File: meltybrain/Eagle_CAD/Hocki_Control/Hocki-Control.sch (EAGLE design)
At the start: 113 parts, among them J1 SM03B-SRSS-TB(LF)(SN), J2 SM03B-SRSS-TB(LF)(SN), U1 TEENSY_4.1, U10 TLV3502AIDCNR, U11 NL27WZ32USG, U12 NL27WZ32USG, U13 HMC1052L-TR, U14 LMV358, U15 IRF7509, U16 TMUX1219DCKR, U17 LMV358, U18 LMV358, U19 AP2210K-3.3TRG1, U2 ADXL375, U20 AP2210K-5.0TRG1, U21 MAX20075ATCA/V+, U3 ADXL375, U4 ADXL375, U5 ADXL375, U6 LMH6612MAX/NOPB, U7 LMH6612MAX/NOPB, U8 LMH6612MAX/NOPB, U9 LMH6612MAX/NOPB

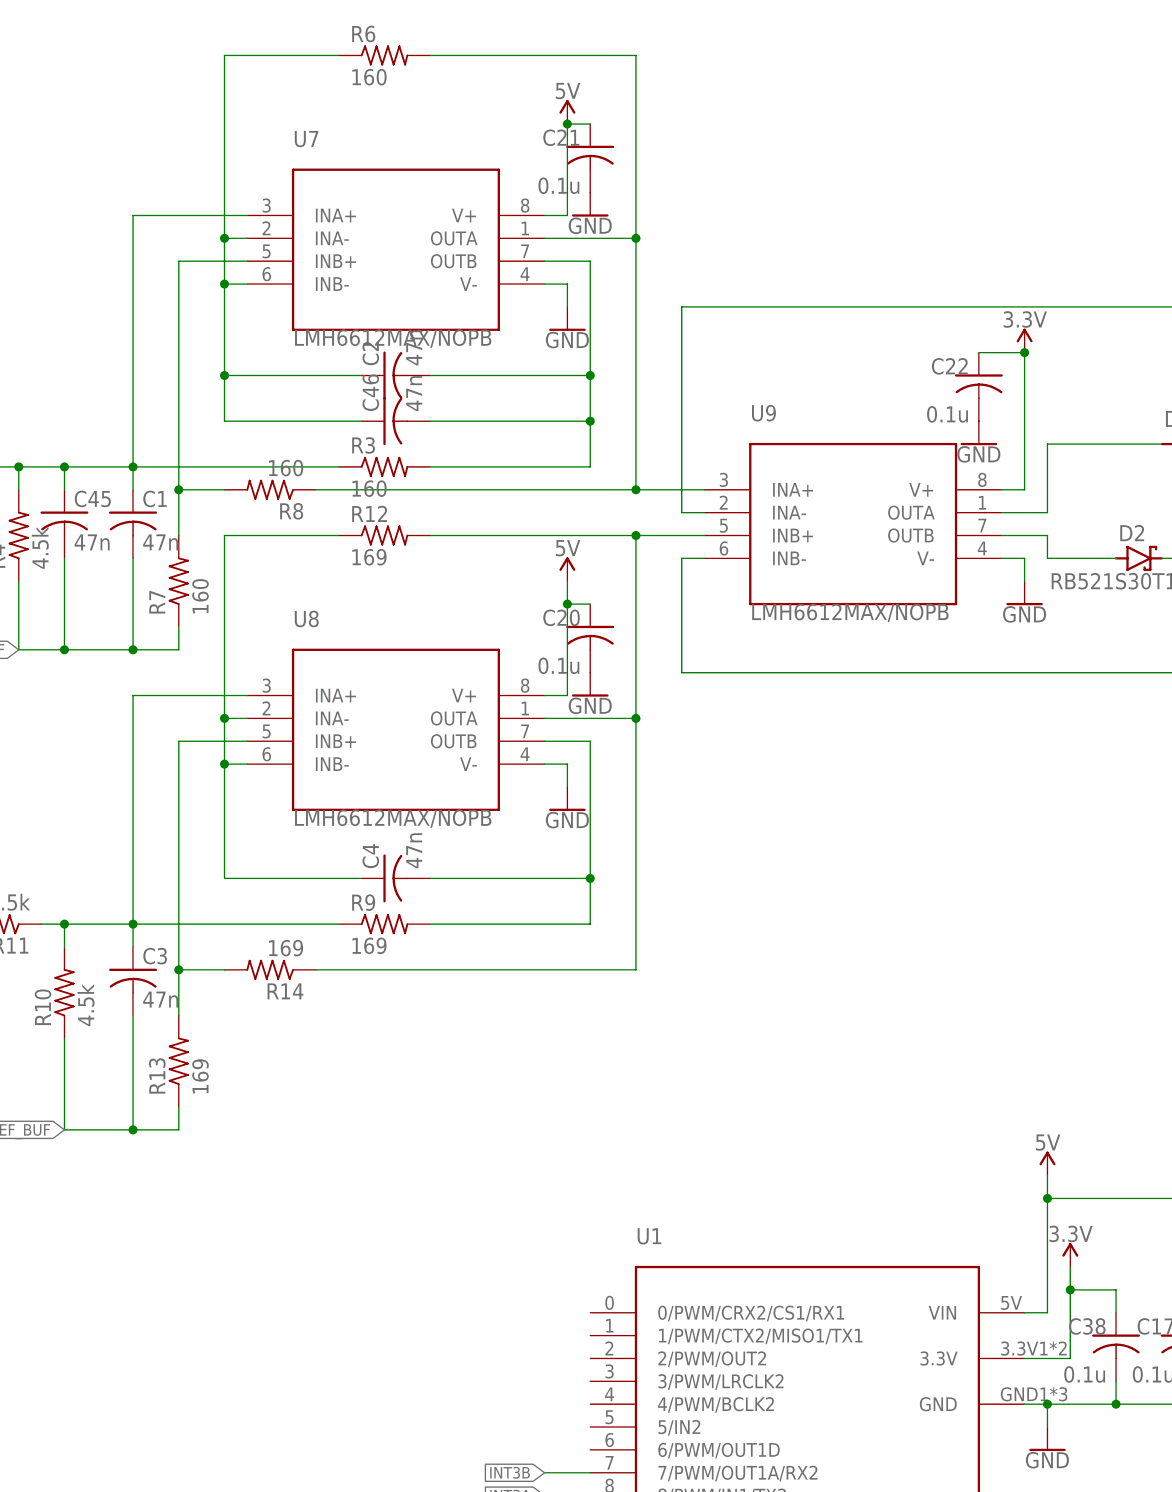
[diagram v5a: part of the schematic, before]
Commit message: errr---added a connector
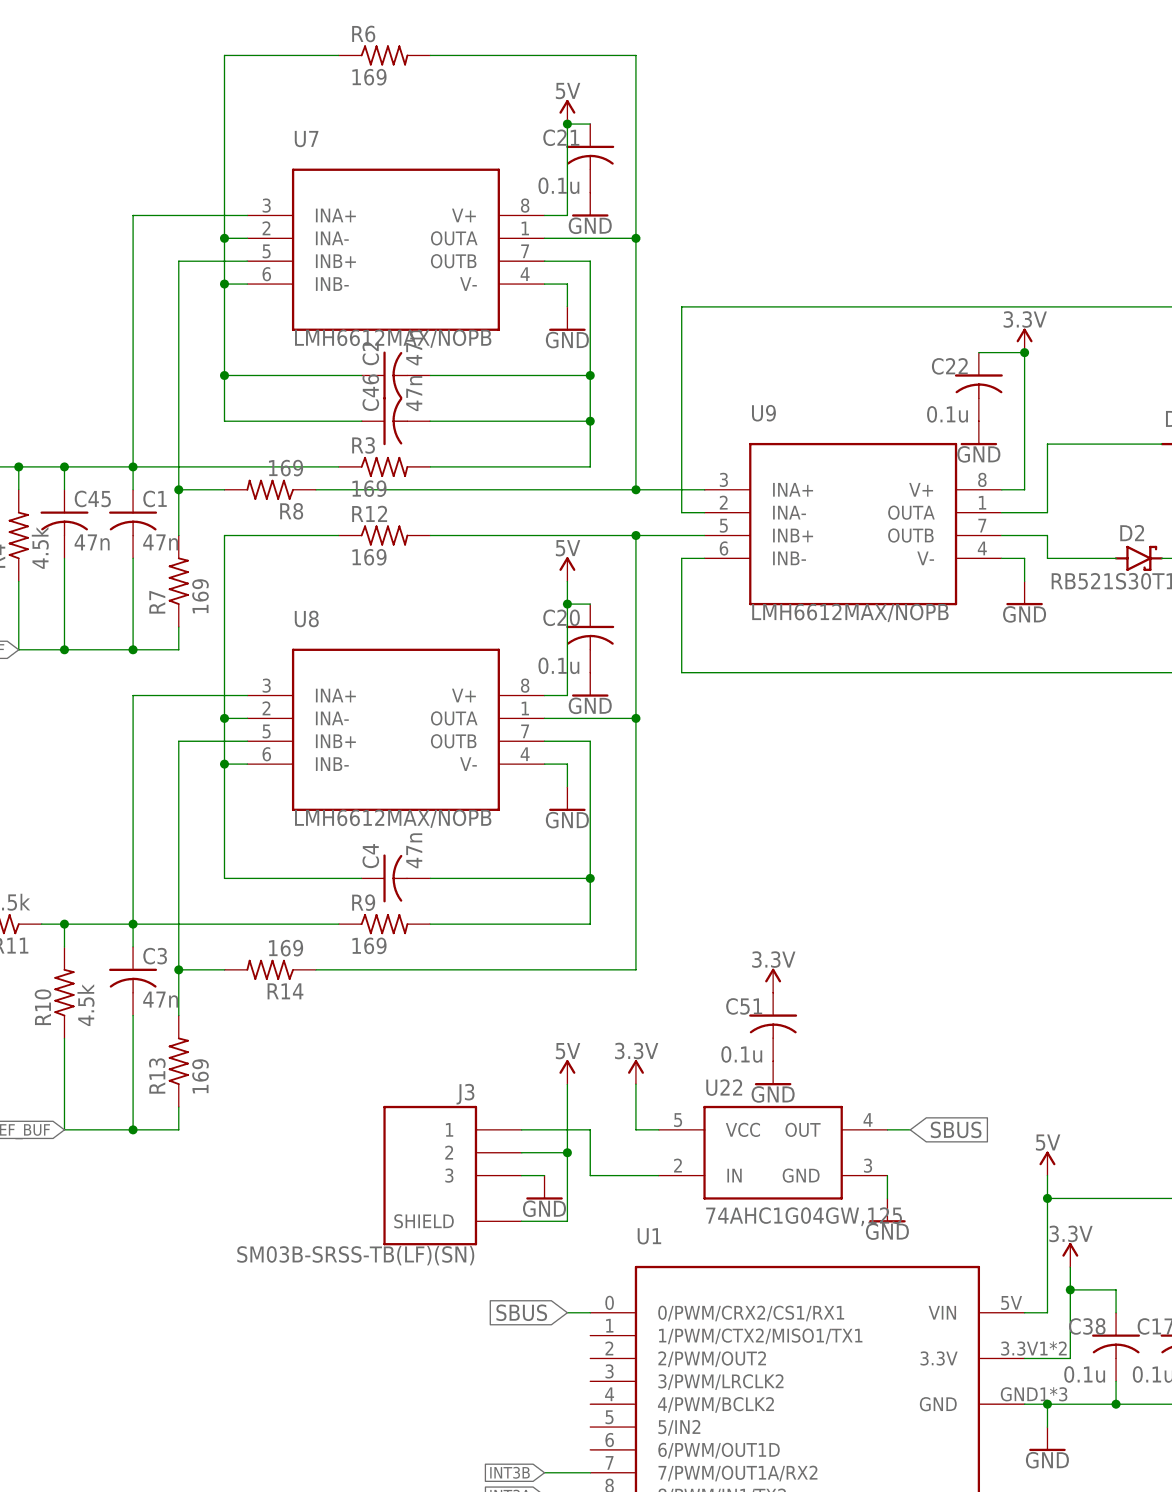
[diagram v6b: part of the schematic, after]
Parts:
- added C51: 0.1u, rcl:C-USC0603
- added J3: SM03B-SRSS-TB(LF)(SN), Hocki_Library:SM03B-SRSS-TB(LF)(SN)
- added U22: 74AHC1G04GW,125, Hocki_Library:74AHC1G04GW,125
- R3, R6, R7, R8: value 160 -> 169
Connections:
- new net N$17: J3.1, U22.IN
- new net SBUS: U1.0/PWM/CRX2/CS1/RX1, U22.OUT
- net 3.3V: now also C51.1, U22.VCC
- net 5V: now also J3.2, J3.SHIELD
- net GND: now also C51.2, J3.3, U22.GND
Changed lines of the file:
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@@
 <part name="SUPPLY5" library="SparkFun-PowerSymbols" library_urn="urn:adsk.eagle:library:530" deviceset="5V" device=""/>
 <part name="GND5" library="SparkFun-PowerSymbols" library_urn="urn:adsk.eagle:library:530" deviceset="GND" device=""/>
-<part name="R3" library="rcl" library_urn="urn:adsk.eagle:library:334" deviceset="R-US_" device="R0603" package3d_urn="urn:adsk.eagle:package:23555/3" value="160"/>
+<part name="R3" library="rcl" library_urn="urn:adsk.eagle:library:334" deviceset="R-US_" device="R0603" package3d_urn="urn:adsk.eagle:package:23555/3" value="169"/>
 <part name="R4" library="rcl" library_urn="urn:adsk.eagle:library:334" deviceset="R-US_" device="R0603" package3d_urn="urn:adsk.eagle:package:23555/3" value="4.5k"/>
 <part name="R5" library="rcl" library_urn="urn:adsk.eagle:library:334" deviceset="R-US_" device="R0603" package3d_urn="urn:adsk.eagle:package:23555/3" value="4.5k"/>
 <part name="GND7" library="SparkFun-PowerSymbols" library_urn="urn:adsk.eagle:library:530" deviceset="GND" device=""/>
 <part name="SUPPLY6" library="SparkFun-PowerSymbols" library_urn="urn:adsk.eagle:library:530" deviceset="5V" device=""/>
-<part name="R6" library="rcl" library_urn="urn:adsk.eagle:library:334" deviceset="R-US_" device="R0603" package3d_urn="urn:adsk.eagle:package:23555/3" value="160"/>
-<part name="R7" library="rcl" library_urn="urn:adsk.eagle:library:334" deviceset="R-US_" device="R0603" package3d_urn="urn:adsk.eagle:package:23555/3" value="160"/>
-<part name="R8" library="rcl" library_urn="urn:adsk.eagle:library:334" deviceset="R-US_" device="R0603" package3d_urn="urn:adsk.eagle:package:23555/3" value="160"/>
+<part name="R6" library="rcl" library_urn="urn:adsk.eagle:library:334" deviceset="R-US_" device="R0603" package3d_urn="urn:adsk.eagle:package:23555/3" value="169"/>
+<part name="R7" library="rcl" library_urn="urn:adsk.eagle:library:334" deviceset="R-US_" device="R0603" package3d_urn="urn:adsk.eagle:package:23555/3" value="169"/>
+<part name="R8" library="rcl" library_urn="urn:adsk.eagle:library:334" deviceset="R-US_" device="R0603" package3d_urn="urn:adsk.eagle:package:23555/3" value="169"/>
 <part name="U8" library="Hocki_Library" deviceset="LMH6612MAX/NOPB" device=""/>
 <part name="R9" library="rcl" library_urn="urn:adsk.eagle:library:334" deviceset="R-US_" device="R0603" package3d_urn="urn:adsk.eagle:package:23555/3" value="169"/>
@@
 <part name="GND59" library="SparkFun-PowerSymbols" library_urn="urn:adsk.eagle:library:530" deviceset="GND" device=""/>
 <part name="SUPPLY22" library="Hocki_Library" deviceset="9V" device=""/>
+<part name="J3" library="Hocki_Library" deviceset="SM03B-SRSS-TB(LF)(SN)" device=""/>
+<part name="GND60" library="SparkFun-PowerSymbols" library_urn="urn:adsk.eagle:library:530" deviceset="GND" device=""/>
+<part name="SUPPLY23" library="SparkFun-PowerSymbols" library_urn="urn:adsk.eagle:library:530" deviceset="5V" device=""/>
+<part name="U22" library="Hocki_Library" deviceset="74AHC1G04GW,125" device=""/>
+<part name="SUPPLY24" library="SparkFun-PowerSymbols" library_urn="urn:adsk.eagle:library:530" deviceset="3.3V" device=""/>
+<part name="GND61" library="SparkFun-PowerSymbols" library_urn="urn:adsk.eagle:library:530" deviceset="GND" device=""/>
+<part name="C51" library="rcl" library_urn="urn:adsk.eagle:library:334" deviceset="C-US" device="C0603" package3d_urn="urn:adsk.eagle:package:23616/2" value="0.1u"/>
+<part name="SUPPLY25" library="SparkFun-PowerSymbols" library_urn="urn:adsk.eagle:library:530" deviceset="3.3V" device=""/>
+<part name="GND62" library="SparkFun-PowerSymbols" library_urn="urn:adsk.eagle:library:530" deviceset="GND" device=""/>
 </parts>
 <sheets>
@@
 <instance part="SUPPLY22" gate="G$1" x="231.14" y="55.88" smashed="yes">
 <attribute name="VALUE" x="231.14" y="58.674" size="1.778" layer="96" align="bottom-center"/>
+</instance>
+<instance part="J3" gate="G$1" x="243.84" y="205.74" smashed="yes" rot="MR0">
+<attribute name="NAME" x="248.92" y="214.122" size="1.778" layer="95" rot="MR0"/>
+<attribute name="VALUE" x="248.92" y="197.866" size="1.778" layer="96" rot="MR0" align="top-left"/>
+</instance>
+<instance part="GND60" gate="1" x="256.54" y="203.2" smashed="yes">
+<attribute name="VALUE" x="256.54" y="202.946" size="1.778" layer="96" align="top-center"/>
+</instance>
+<instance part="SUPPLY23" gate="G$1" x="259.08" y="215.9" smashed="yes">
+<attribute name="VALUE" x="259.08" y="218.694" size="1.778" layer="96" align="bottom-center"/>
+</instance>
+<instance part="U22" gate="G$1" x="281.94" y="210.82" smashed="yes">
+<attribute name="NAME" x="274.32" y="214.63" size="1.778" layer="95" ratio="6" rot="SR0"/>
+<attribute name="VALUE" x="274.32" y="202.184" size="1.778" layer="96" ratio="6" rot="SR0" align="top-left"/>
+</instance>
+<instance part="SUPPLY24" gate="G$1" x="266.7" y="215.9" smashed="yes">
+<attribute name="VALUE" x="266.7" y="218.694" size="1.778" layer="96" align="bottom-center"/>
+</instance>
+<instance part="GND61" gate="1" x="294.64" y="200.66" smashed="yes">
+<attribute name="VALUE" x="294.64" y="200.406" size="1.778" layer="96" align="top-center"/>
+</instance>
+<instance part="C51" gate="G$1" x="281.94" y="223.52" smashed="yes">
+<attribute name="NAME" x="280.924" y="225.425" size="1.778" layer="95" rot="R180"/>
+<attribute name="VALUE" x="280.924" y="220.091" size="1.778" layer="96" rot="R180"/>
+</instance>
+<instance part="SUPPLY25" gate="G$1" x="281.94" y="226.06" smashed="yes">
+<attribute name="VALUE" x="281.94" y="228.854" size="1.778" layer="96" align="bottom-center"/>
+</instance>
+<instance part="GND62" gate="1" x="281.94" y="215.9" smashed="yes">
+<attribute name="VALUE" x="281.94" y="215.646" size="1.778" layer="96" align="top-center"/>
 </instance>
 </instances>
@@
 <pinref part="GND59" gate="1" pin="GND"/>
 </segment>
+<segment>
+<pinref part="J3" gate="G$1" pin="3"/>
+<wire x1="254" y1="205.74" x2="256.54" y2="205.74" width="0.1524" layer="91"/>
+<pinref part="GND60" gate="1" pin="GND"/>
+</segment>
+<segment>
+<pinref part="U22" gate="G$1" pin="GND"/>
+<wire x1="294.64" y1="205.74" x2="294.64" y2="203.2" width="0.1524" layer="91"/>
+<pinref part="GND61" gate="1" pin="GND"/>
+</segment>
+<segment>
+<pinref part="C51" gate="G$1" pin="2"/>
+<pinref part="GND62" gate="1" pin="GND"/>
+</segment>
 </net>
 <net name="3.3V" class="0">
@@
 <wire x1="320.04" y1="193.04" x2="314.96" y2="193.04" width="0.1524" layer="91"/>
 <junction x="314.96" y="193.04"/>
+</segment>
+<segment>
+<pinref part="U22" gate="G$1" pin="VCC"/>
+<wire x1="269.24" y1="210.82" x2="266.7" y2="210.82" width="0.1524" layer="91"/>
+<wire x1="266.7" y1="210.82" x2="266.7" y2="215.9" width="0.1524" layer="91"/>
+<pinref part="SUPPLY24" gate="G$1" pin="3.3V"/>
+</segment>
+<segment>
+<pinref part="C51" gate="G$1" pin="1"/>
+<pinref part="SUPPLY25" gate="G$1" pin="3.3V"/>
 </segment>
 </net>
@@
 <pinref part="SUPPLY20" gate="G$1" pin="5V"/>
 </segment>
+<segment>
+<pinref part="J3" gate="G$1" pin="2"/>
+<wire x1="254" y1="208.28" x2="259.08" y2="208.28" width="0.1524" layer="91"/>
+<wire x1="259.08" y1="208.28" x2="259.08" y2="215.9" width="0.1524" layer="91"/>
+<pinref part="SUPPLY23" gate="G$1" pin="5V"/>
+<pinref part="J3" gate="G$1" pin="SHIELD"/>
+<wire x1="254" y1="200.66" x2="259.08" y2="200.66" width="0.1524" layer="91"/>
+<wire x1="259.08" y1="200.66" x2="259.08" y2="208.28" width="0.1524" layer="91"/>
+<junction x="259.08" y="208.28"/>
+</segment>
 </net>
 <net name="VG_SIGNAL_BUF" class="0">
@@
 </segment>
 </net>
+<net name="N$17" class="0">
+<segment>
+<pinref part="J3" gate="G$1" pin="1"/>
+<wire x1="254" y1="210.82" x2="261.62" y2="210.82" width="0.1524" layer="91"/>
+<wire x1="261.62" y1="210.82" x2="261.62" y2="205.74" width="0.1524" layer="91"/>
+<pinref part="U22" gate="G$1" pin="IN"/>
+<wire x1="261.62" y1="205.74" x2="269.24" y2="205.74" width="0.1524" layer="91"/>
+</segment>
+</net>
+<net name="SBUS" class="0">
+<segment>
+<pinref part="U22" gate="G$1" pin="OUT"/>
+<wire x1="294.64" y1="210.82" x2="297.18" y2="210.82" width="0.1524" layer="91"/>
+<label x="297.18" y="210.82" size="1.778" layer="95" xref="yes"/>
+</segment>
+<segment>
+<pinref part="U1" gate="G$1" pin="0/PWM/CRX2/CS1/RX1"/>
+<wire x1="261.62" y1="190.5" x2="259.08" y2="190.5" width="0.1524" layer="91"/>
+<label x="259.08" y="190.5" size="1.778" layer="95" rot="R180" xref="yes"/>
+</segment>
+</net>

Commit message: finished routing control?
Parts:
- added C52: 22u, rcl:C-USC1206
- added C53: 4.7u, rcl:C-USC0603
- added C54: 1u, rcl:C-USC0603
- added CN1: (no value), Hocki_Library:JST_2PIN-SMT-RA
- added J4, J5: SM04B-SRSS-TB(LF)(SN), Hocki_Library:SM04B-SRSS-TB(LF)(SN)
- added U23: LDL212PU50R, Hocki_Library:LDL212PU50R
- C47: value 4.7u -> 10u
- C49: value 1u -> 100p
- L1: value 4.7u -> 10uH; device Hocki_Library:CBC2518T4R7M -> Hocki_Library:LQH5BPN100M38L
- R1: value 324k -> 205k
- R15: value 40.2k -> 20k
- U21: value MAX20075ATCA/V+ -> AP63200; device Hocki_Library:MAX20075ATCA/V+ -> Hocki_Library:AP63200
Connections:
- removed net N$6: C49.1, U21.BIAS
- new net +5V: C53.1, J4.1, J4.SHIELD, J5.1, J5.SHIELD, U23.ADJ/SENSE, U23.OUT
- new net LED_CLK1: J4.2, U1.2/PWM/OUT2
- new net LED_CLK2: J5.2, U1.4/PWM/BCLK2
- new net LED_DATA1: J4.3, U1.1/PWM/CTX2/MISO1/TX1
- new net LED_DATA2: J5.3, U1.3/PWM/LRCLK2
- net +24V: now also CN1.2, CN1.SHIELD, U21.IN; no longer U21.SUP
- net 9V: now also C49.1, C52.1, C54.1, U23.IN; no longer U21.OUT
- net GND: now also C52.2, C53.2, C54.2, CN1.1, J4.4, J5.4, U21.GND, U23.GND; no longer C49.2, U21.AGND, U21.EPAD, U21.PGND
- net N$12: now also C49.2
- net N$3: now also U21.SW; no longer U21.LX
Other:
- moved on the sheet: C47, C48, C49, C50, L1, R1, R15
